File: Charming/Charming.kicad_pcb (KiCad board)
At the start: 2 copper layers, 9 parts, among them SW1 SW_Push, SW2 SW_Push, SW3 SW_Push, SW4 SW_Push, U1 ProMicro

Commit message: keyboard matrix ok
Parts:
- added D10: D, Diode_SMD:D_SOD-123, F.Cu at (156.5, 124.8)
- added D11: D, Diode_SMD:D_SOD-123, F.Cu at (162.3, 121.5)
- added D12: D, Diode_SMD:D_SOD-123, F.Cu at (156.5, 121.5)
- added D13: D, Diode_SMD:D_SOD-123, F.Cu at (150.8, 124.8)
- added D14: D, Diode_SMD:D_SOD-123, F.Cu at (145.0, 124.8)
- added D15: D, Diode_SMD:D_SOD-123, F.Cu at (139.3, 131.5)
- added D16: D, Diode_SMD:D_SOD-123, F.Cu at (150.8, 121.5)
- added D17: D, Diode_SMD:D_SOD-123, F.Cu at (133.5, 131.5)
- added D18: D, Diode_SMD:D_SOD-123, F.Cu at (127.8, 131.5)
- added D19: D, Diode_SMD:D_SOD-123, F.Cu at (139.3, 128.2)
- added D20: D, Diode_SMD:D_SOD-123, F.Cu at (133.5, 128.2)
- added D21: D, Diode_SMD:D_SOD-123, F.Cu at (139.3, 124.8)
- added D22: D, Diode_SMD:D_SOD-123, F.Cu at (145.0, 121.5)
- added D23: D, Diode_SMD:D_SOD-123, F.Cu at (139.3, 121.5)
- added D24: D, Diode_SMD:D_SOD-123, F.Cu at (133.5, 124.8)
- added D25: D, Diode_SMD:D_SOD-123, F.Cu at (127.8, 128.2)
- added D26: D, Diode_SMD:D_SOD-123, F.Cu at (122.0, 131.5)
- added D27: D, Diode_SMD:D_SOD-123, F.Cu at (133.5, 121.5)
- added D28: D, Diode_SMD:D_SOD-123, F.Cu at (116.3, 131.5)
- added D29: D, Diode_SMD:D_SOD-123, F.Cu at (110.5, 131.5)
- added D30: D, Diode_SMD:D_SOD-123, F.Cu at (122.0, 128.2)
- added D31: D, Diode_SMD:D_SOD-123, F.Cu at (116.3, 128.2)
- added D32: D, Diode_SMD:D_SOD-123, F.Cu at (127.8, 124.8)
- added D33: D, Diode_SMD:D_SOD-123, F.Cu at (122.0, 124.8)
- added D34: D, Diode_SMD:D_SOD-123, F.Cu at (127.8, 121.5)
- added D35: D, Diode_SMD:D_SOD-123, F.Cu at (122.0, 121.5)
- added D36: D, Diode_SMD:D_SOD-123, F.Cu at (116.3, 124.8)
- added D37: D, Diode_SMD:D_SOD-123, F.Cu at (110.5, 128.2)
- added D38: D, Diode_SMD:D_SOD-123, F.Cu at (116.3, 121.5)
- added D39: D, Diode_SMD:D_SOD-123, F.Cu at (104.8, 131.5)
- added D40: D, Diode_SMD:D_SOD-123, F.Cu at (99.0, 131.5)
- added D41: D, Diode_SMD:D_SOD-123, F.Cu at (104.8, 128.2)
- added D42: D, Diode_SMD:D_SOD-123, F.Cu at (99.0, 128.2)
- added D43: D, Diode_SMD:D_SOD-123, F.Cu at (110.5, 124.8)
- added D44: D, Diode_SMD:D_SOD-123, F.Cu at (110.5, 121.5)
- added D45: D, Diode_SMD:D_SOD-123, F.Cu at (104.8, 124.8)
- added D46: D, Diode_SMD:D_SOD-123, F.Cu at (99.0, 124.8)
- added D47: D, Diode_SMD:D_SOD-123, F.Cu at (104.8, 121.5)
- added D48: D, Diode_SMD:D_SOD-123, F.Cu at (99.0, 121.5)
- added D5: D, Diode_SMD:D_SOD-123, F.Cu at (150.8, 131.5)
- added D6: D, Diode_SMD:D_SOD-123, F.Cu at (145.0, 131.5)
- added D7: D, Diode_SMD:D_SOD-123, F.Cu at (156.5, 128.2)
- added D8: D, Diode_SMD:D_SOD-123, F.Cu at (150.8, 128.2)
- added D9: D, Diode_SMD:D_SOD-123, F.Cu at (145.0, 128.2)
- added SW10: SW_Push, keyswitches:SW_PG1350, F.Cu at (218.5, 38.0)
- added SW11: SW_Push, keyswitches:SW_PG1350, F.Cu at (237.5, 38.0)
- added SW12: SW_Push, keyswitches:SW_PG1350, F.Cu at (256.5, 38.0)
- added SW13: SW_Push, keyswitches:SW_PG1350, F.Cu at (42.8, 57.0)
- added SW14: SW_Push, keyswitches:SW_PG1350, F.Cu at (61.8, 57.0)
- added SW15: SW_Push, keyswitches:SW_PG1350, F.Cu at (80.8, 57.0)
- added SW16: SW_Push, keyswitches:SW_PG1350, F.Cu at (99.8, 57.0)
- added SW17: SW_Push, keyswitches:SW_PG1350, F.Cu at (118.8, 57.0)
- added SW18: SW_Push, keyswitches:SW_PG1350, F.Cu at (137.8, 57.0)
- added SW19: SW_Push, keyswitches:SW_PG1350, F.Cu at (166.2, 57.0)
- added SW20: SW_Push, keyswitches:SW_PG1350, F.Cu at (185.2, 57.0)
- added SW21: SW_Push, keyswitches:SW_PG1350, F.Cu at (204.2, 57.0)
- added SW22: SW_Push, keyswitches:SW_PG1350, F.Cu at (223.2, 57.0)
- added SW23: SW_Push, keyswitches:SW_PG1350, F.Cu at (242.2, 57.0)
- added SW24: SW_Push, keyswitches:SW_PG1350, F.Cu at (261.2, 57.0)
- added SW25: SW_Push, keyswitches:SW_PG1350, F.Cu at (38.0, 76.0)
- added SW26: SW_Push, keyswitches:SW_PG1350, F.Cu at (57.0, 76.0)
- added SW27: SW_Push, keyswitches:SW_PG1350, F.Cu at (76.0, 76.0)
- added SW28: SW_Push, keyswitches:SW_PG1350, F.Cu at (95.0, 76.0)
- added SW29: SW_Push, keyswitches:SW_PG1350, F.Cu at (114.0, 76.0)
- added SW30: SW_Push, keyswitches:SW_PG1350, F.Cu at (133.0, 76.0)
- added SW31: SW_Push, keyswitches:SW_PG1350, F.Cu at (171.0, 76.0)
- added SW32: SW_Push, keyswitches:SW_PG1350, F.Cu at (190.0, 76.0)
- added SW33: SW_Push, keyswitches:SW_PG1350, F.Cu at (209.0, 76.0)
- added SW34: SW_Push, keyswitches:SW_PG1350, F.Cu at (228.0, 76.0)
- added SW35: SW_Push, keyswitches:SW_PG1350, F.Cu at (247.0, 76.0)
- added SW36: SW_Push, keyswitches:SW_PG1350, F.Cu at (266.0, 76.0)
- added SW37: SW_Push, keyswitches:SW_PG1350, F.Cu at (47.5, 95.0)
- added SW38: SW_Push, keyswitches:SW_PG1350, F.Cu at (66.5, 95.0)
- added SW39: SW_Push, keyswitches:SW_PG1350, F.Cu at (85.5, 95.0)
- added SW40: SW_Push, keyswitches:SW_PG1350, F.Cu at (104.5, 95.0)
- added SW41: SW_Push, keyswitches:SW_PG1350, F.Cu at (128.2, 95.0)
- added SW42: SW_Push, keyswitches:SW_PG1350, F.Cu at (152.0, 76.0)
- added SW43: SW_Push, keyswitches:SW_PG1350, F.Cu at (152.0, 95.0)
- added SW44: SW_Push, keyswitches:SW_PG1350, F.Cu at (175.8, 95.0)
- added SW45: SW_Push, keyswitches:SW_PG1350, F.Cu at (199.5, 95.0)
- added SW46: SW_Push, keyswitches:SW_PG1350, F.Cu at (218.5, 95.0)
- added SW47: SW_Push, keyswitches:SW_PG1350, F.Cu at (237.5, 95.0)
- added SW48: SW_Push, keyswitches:SW_PG1350, F.Cu at (256.5, 95.0)
- added SW5: SW_Push, keyswitches:SW_PG1350, F.Cu at (123.5, 38.0)
- added SW6: SW_Push, keyswitches:SW_PG1350, F.Cu at (142.5, 38.0)
- added SW7: SW_Push, keyswitches:SW_PG1350, F.Cu at (161.5, 38.0)
- added SW8: SW_Push, keyswitches:SW_PG1350, F.Cu at (180.5, 38.0)
- added SW9: SW_Push, keyswitches:SW_PG1350, F.Cu at (199.5, 38.0)
- moved SW1 152.4 mm to (47.5, 38.0)
- moved SW2 151.9 mm to (66.5, 38.0)
- moved U1 146.2 mm to (19.0, 52.2)
- moved SW4 140.1 mm to (104.5, 38.0)
- moved SW3 138.1 mm to (85.5, 38.0)
- moved D4 31.3 mm to (168.0, 121.5), turned to 0 degrees
- moved D2 27.5 mm to (162.3, 124.8), turned to 0 degrees
- moved D3 19.4 mm to (156.5, 131.5), turned to 0 degrees
- moved D1 13.7 mm to (168.0, 124.8), turned to 0 degrees
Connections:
- D2 pad 1: row1 -> row0
- D4 pad 1: row1 -> row0
- SW2 pad 1: col0 -> col1
- SW3 pad 1: col1 -> col2
- SW4 pad 1: col1 -> col3
- U1 pad 10: Net-(U1-Pad10) -> col6
- U1 pad 11: Net-(U1-Pad11) -> col5
- U1 pad 12: Net-(U1-Pad12) -> col4
- U1 pad 13: Net-(U1-Pad13) -> col3
- U1 pad 14: Net-(U1-Pad14) -> col2
- U1 pad 15: Net-(U1-Pad15) -> col1
- U1 pad 16: Net-(U1-Pad16) -> col0
- U1 pad 17: col1 -> row3
- U1 pad 18: col0 -> row2
- U1 pad 5: Net-(U1-Pad5) -> col11
- U1 pad 6: Net-(U1-Pad6) -> col10
- U1 pad 7: Net-(U1-Pad7) -> col9
- U1 pad 8: Net-(U1-Pad8) -> col8
- U1 pad 9: Net-(U1-Pad9) -> col7
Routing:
- net col1: track 70.4 -> 0.00 mm
- net col0: track 50.9 -> 0.00 mm
- net row1: track 37.3 -> 0.00 mm
- net row0: track 35.5 -> 0.00 mm
- net GND: track 18.8 -> 0.00 mm
- net Net-(D2-Pad2): track 6.06 -> 0.00 mm
- net Net-(D1-Pad2): track 5.83 -> 0.00 mm
- net Net-(D4-Pad2): track 5.68 -> 0.00 mm
- net Net-(D3-Pad2): track 5.68 -> 0.00 mm

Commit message: all components on but routing failed
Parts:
- moved D1 160.0 mm to (41.4, 27.0), turned to 270 degrees
- moved D36 153.6 mm to (259.9, 70.2), turned to 270 degrees
- moved D48 150.2 mm to (248.4, 105.8), turned to 270 degrees
- moved D2 144.9 mm to (55.4, 27.0), turned to 270 degrees
- moved D24 138.9 mm to (249.7, 48.6), turned to 270 degrees
- moved D13 137.9 mm to (35.1, 49.9), turned to 270 degrees
- moved D12 132.7 mm to (249.7, 27.0), turned to 270 degrees
- moved D3 132.1 mm to (75.7, 27.0), turned to 270 degrees
- moved D35 130.5 mm to (242.1, 70.2), turned to 270 degrees
- moved D47 128.1 mm to (231.9, 105.8), turned to 270 degrees
- moved D46 121.7 mm to (219.2, 105.8), turned to 270 degrees
- moved D4 120.3 mm to (93.5, 27.0), turned to 270 degrees
- moved D14 117.8 mm to (54.1, 49.9), turned to 270 degrees
- moved D23 116.9 mm to (230.6, 48.6), turned to 270 degrees
- moved D11 116.6 mm to (230.6, 27.0), turned to 270 degrees
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
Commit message: 3d view is back
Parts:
- D1, D10, D11, D12, D2, D3, D4, D5, D6, D7, D8, D9: moved to B.Cu
- moved D6 2.54 mm to (135.4, 25.8), turned to 90 degrees
- turned D1 to 90 degrees
- turned D10 to 90 degrees
- turned D11 to 90 degrees
- turned D12 to 90 degrees
- turned D2 to 90 degrees
- turned D3 to 90 degrees
- turned D4 to 90 degrees
- turned D5 to 90 degrees
- turned D7 to 90 degrees
- turned D8 to 90 degrees
- turned D9 to 90 degrees
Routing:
- net row3: track 0.00 -> 341.4 mm, vias 0 -> 1
- net col11: track 0.00 -> 315.3 mm
- net row0: track 0.00 -> 303.2 mm
- net col10: track 0.00 -> 293.6 mm
- net col9: track 0.00 -> 275.3 mm
- net row2: track 0.00 -> 260.1 mm, vias 0 -> 1
- net col8: track 0.00 -> 254.9 mm
- net col7: track 0.00 -> 247.1 mm
- net row1: track 0.00 -> 230.8 mm, vias 0 -> 1
- net col6: track 0.00 -> 230.3 mm
- net col5: track 0.00 -> 191.3 mm
- net col4: track 0.00 -> 177.8 mm
- net col3: track 0.00 -> 141.8 mm
- net col2: track 0.00 -> 123.7 mm
- net col1: track 0.00 -> 100.3 mm
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
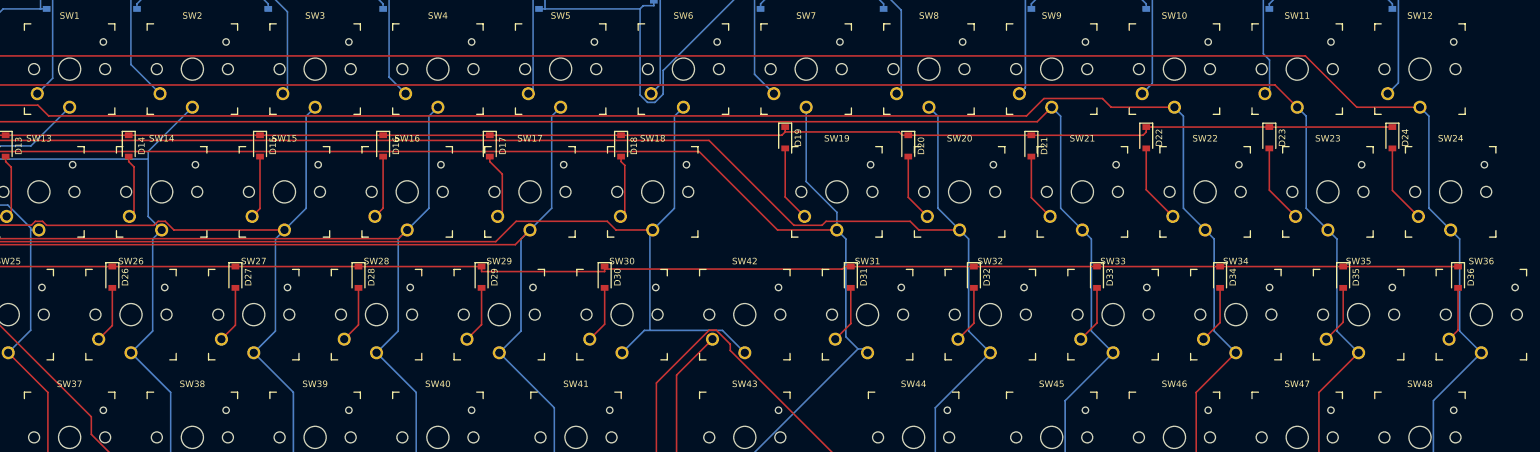
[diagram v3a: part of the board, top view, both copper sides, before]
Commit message: update PG13500 footprint
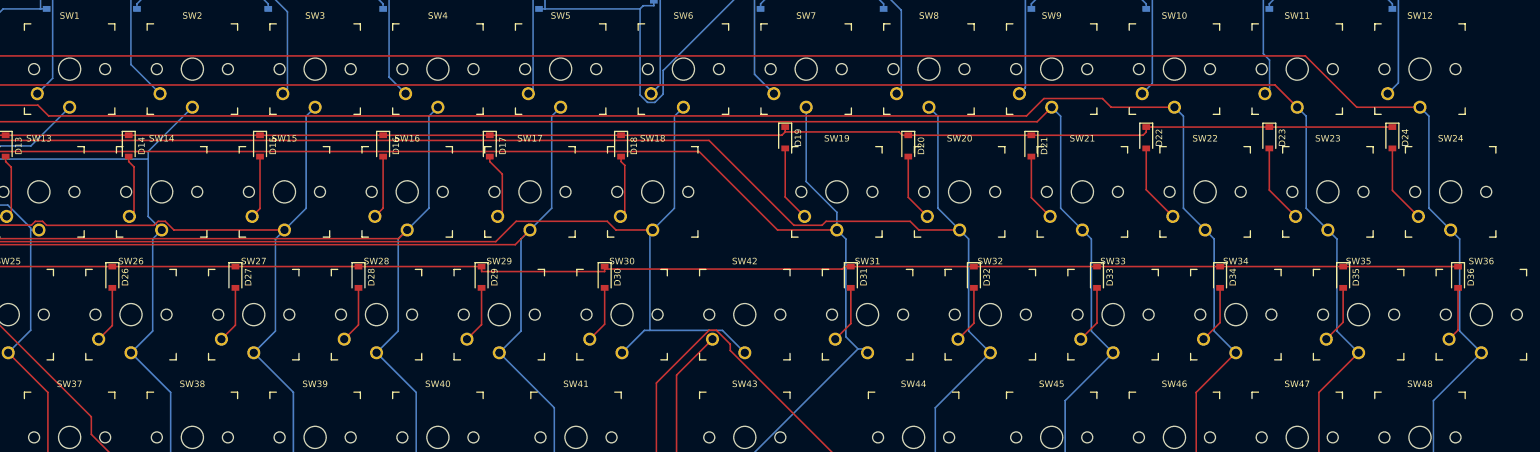
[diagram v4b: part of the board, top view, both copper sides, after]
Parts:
- SW1, SW10, SW11, SW12, SW13, SW14, SW15, SW16, SW17, SW18, SW19, SW2, SW20, SW21, SW22, SW23, SW24, SW25, SW26, SW27, SW28, SW29, SW3, SW30, SW31, SW32, SW33, SW34, SW35, SW36, SW37, SW38, SW39, SW4, SW40, SW41, SW42, SW43, SW44, SW45, SW46, SW47, SW48, SW5, SW6, SW7, SW8, SW9: footprint keyswitches:SW_PG1350 -> Charming:SW_PG1350
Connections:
- D10 pad 1: row0 -> row1
- D11 pad 1: row0 -> row2
- D12 pad 1: row0 -> row3
- D13 pad 1: row1 -> row0
- D15 pad 1: row1 -> row2
- D16 pad 1: row1 -> row3
- D17 pad 1: row1 -> row0
- D19 pad 1: row1 -> row2
- D2 pad 1: row0 -> row1
- D20 pad 1: row1 -> row3
- D21 pad 1: row1 -> row0
- D23 pad 1: row1 -> row2
- D24 pad 1: row1 -> row3
- D25 pad 1: row2 -> row0
- D26 pad 1: row2 -> row1
- D28 pad 1: row2 -> row3
- D29 pad 1: row2 -> row0
- D3 pad 1: row0 -> row2
- D30 pad 1: row2 -> row1
- D32 pad 1: row2 -> row3
- D33 pad 1: row2 -> row0
- D34 pad 1: row2 -> row1
- D36 pad 1: row2 -> row3
- D37 pad 1: row3 -> row0
- D38 pad 1: row3 -> row1
- D39 pad 1: row3 -> row2
- D4 pad 1: row0 -> row3
- D41 pad 1: row3 -> row0
- D42 pad 1: row3 -> row1
- D43 pad 1: row3 -> row2
- D45 pad 1: row3 -> row0
- D46 pad 1: row3 -> row1
- D47 pad 1: row3 -> row2
- D6 pad 1: row0 -> row1
- D7 pad 1: row0 -> row2
- D8 pad 1: row0 -> row3
- SW10 pad 1: col9 -> col2
- SW11 pad 1: col10 -> col2
- SW12 pad 1: col11 -> col2
- SW13 pad 1: col0 -> col3
- SW14 pad 1: col1 -> col3
- SW15 pad 1: col2 -> col3
- SW18 pad 1: col5 -> col4
- SW19 pad 1: col6 -> col4
- SW2 pad 1: col1 -> col0
- SW20 pad 1: col7 -> col4
- SW21 pad 1: col8 -> col5
- SW22 pad 1: col9 -> col5
- SW23 pad 1: col10 -> col5
- SW24 pad 1: col11 -> col5
- SW25 pad 1: col0 -> col6
- SW26 pad 1: col1 -> col6
- SW27 pad 1: col2 -> col6
- SW28 pad 1: col3 -> col6
- SW29 pad 1: col4 -> col7
- SW3 pad 1: col2 -> col0
- SW30 pad 1: col5 -> col7
- SW31 pad 1: col6 -> col7
- SW34 pad 1: col9 -> col8
- SW35 pad 1: col10 -> col8
- SW36 pad 1: col11 -> col8
- SW37 pad 1: col0 -> col9
- SW38 pad 1: col1 -> col9
- SW39 pad 1: col2 -> col9
- SW4 pad 1: col3 -> col0
- SW40 pad 1: col3 -> col9
- SW41 pad 1: col4 -> col10
- SW42 pad 1: col5 -> col10
- SW43 pad 1: col6 -> col10
- SW44 pad 1: col7 -> col10
- SW45 pad 1: col8 -> col11
- SW46 pad 1: col9 -> col11
- SW47 pad 1: col10 -> col11
- SW5 pad 1: col4 -> col1
- SW6 pad 1: col5 -> col1
- SW7 pad 1: col6 -> col1
- SW8 pad 1: col7 -> col1
- SW9 pad 1: col8 -> col2

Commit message: before row col changle
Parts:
- D1, D10, D11, D12, D2, D3, D4, D5, D6, D7, D8, D9: moved to F.Cu
- moved D42 32.2 mm to (140.0, 73.6)
- moved D43 26.8 mm to (140.0, 92.6)
- moved D37 22.1 mm to (35.5, 92.6)
- moved D40 21.6 mm to (92.5, 92.6)
- moved D39 21.1 mm to (73.5, 92.6)
- moved D38 21.1 mm to (54.5, 92.6)
- moved D41 20.5 mm to (111.5, 92.6)
- moved D44 19.0 mm to (166.1, 92.6)
- moved D46 18.3 mm to (206.5, 92.6)
- moved D45 18.3 mm to (187.5, 92.6)
- moved D47 14.6 mm to (225.5, 92.6)
- moved D48 13.7 mm to (244.5, 92.6)
- moved D6 10.8 mm to (130.5, 35.4), turned to 270 degrees
- moved D9 10.5 mm to (187.5, 35.4), turned to 270 degrees
- moved D1 10.4 mm to (35.2, 35.4), turned to 270 degrees
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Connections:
- D10 pad 1: row1 -> row0
- D11 pad 1: row2 -> row0
- D12 pad 1: row3 -> row0
- D13 pad 1: row0 -> row1
- D15 pad 1: row2 -> row1
- D16 pad 1: row3 -> row1
- D17 pad 1: row0 -> row1
- D19 pad 1: row2 -> row1
- D2 pad 1: row1 -> row0
- D20 pad 1: row3 -> row1
- D21 pad 1: row0 -> row1
- D23 pad 1: row2 -> row1
- D24 pad 1: row3 -> row1
- D25 pad 1: row0 -> row2
- D26 pad 1: row1 -> row2
- D28 pad 1: row3 -> row2
- D29 pad 1: row0 -> row2
- D3 pad 1: row2 -> row0
- D30 pad 1: row1 -> row2
- D32 pad 1: row3 -> row2
- D33 pad 1: row0 -> row2
- D34 pad 1: row1 -> row2
- D36 pad 1: row3 -> row2
- D37 pad 1: row0 -> row3
- D38 pad 1: row1 -> row3
- D39 pad 1: row2 -> row3
- D4 pad 1: row3 -> row0
- D41 pad 1: row0 -> row3
- D42 pad 1: row1 -> row3
- D43 pad 1: row2 -> row3
- D45 pad 1: row0 -> row3
- D46 pad 1: row1 -> row3
- D47 pad 1: row2 -> row3
- D6 pad 1: row1 -> row0
- D7 pad 1: row2 -> row0
- D8 pad 1: row3 -> row0
- SW10 pad 1: col2 -> col9
- SW11 pad 1: col2 -> col10
- SW12 pad 1: col2 -> col11
- SW13 pad 1: col3 -> col0
- SW14 pad 1: col3 -> col1
- SW15 pad 1: col3 -> col2
- SW18 pad 1: col4 -> col5
- SW19 pad 1: col4 -> col6
- SW2 pad 1: col0 -> col1
- SW20 pad 1: col4 -> col7
- SW21 pad 1: col5 -> col8
- SW22 pad 1: col5 -> col9
- SW23 pad 1: col5 -> col10
- SW24 pad 1: col5 -> col11
- SW25 pad 1: col6 -> col0
- SW26 pad 1: col6 -> col1
- SW27 pad 1: col6 -> col2
- SW28 pad 1: col6 -> col3
- SW29 pad 1: col7 -> col4
- SW3 pad 1: col0 -> col2
- SW30 pad 1: col7 -> col5
- SW31 pad 1: col7 -> col6
- SW34 pad 1: col8 -> col9
- SW35 pad 1: col8 -> col10
- SW36 pad 1: col8 -> col11
- SW37 pad 1: col9 -> col0
- SW38 pad 1: col9 -> col1
- SW39 pad 1: col9 -> col2
- SW4 pad 1: col0 -> col3
- SW40 pad 1: col9 -> col3
- SW41 pad 1: col10 -> col4
- SW42 pad 1: col10 -> col5
- SW43 pad 1: col10 -> col6
- SW44 pad 1: col10 -> col7
- SW45 pad 1: col11 -> col8
- SW46 pad 1: col11 -> col9
- SW47 pad 1: col11 -> col10
- SW5 pad 1: col1 -> col4
- SW6 pad 1: col1 -> col5
- SW7 pad 1: col1 -> col6
- SW8 pad 1: col1 -> col7
- SW9 pad 1: col2 -> col8
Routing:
- net row3: track 341.4 -> 0.00 mm, vias 1 -> 0
- net col11: track 315.3 -> 0.00 mm
- net row0: track 303.2 -> 0.00 mm
- net col10: track 293.6 -> 0.00 mm
- net col9: track 275.3 -> 0.00 mm
- net row2: track 260.1 -> 0.00 mm, vias 1 -> 0
- net col8: track 254.9 -> 0.00 mm
- net col7: track 247.1 -> 0.00 mm
- net row1: track 230.8 -> 0.00 mm, vias 1 -> 0
- net col6: track 230.3 -> 0.00 mm
- net col5: track 191.3 -> 0.00 mm
- net col4: track 177.8 -> 0.00 mm
- net col3: track 141.8 -> 0.00 mm
- net col2: track 123.7 -> 0.00 mm
- net col1: track 100.3 -> 0.00 mm
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
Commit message: v1
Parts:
- moved D29 46.5 mm to (131.5, 109.6)
- moved D30 46.5 mm to (150.5, 109.6)
- moved D25 46.5 mm to (55.5, 109.6)
- moved D28 46.5 mm to (112.5, 109.6)
- moved D26 46.5 mm to (74.5, 109.6)
- moved D27 46.5 mm to (93.5, 109.6)
- moved D42 45.9 mm to (150.5, 118.3), turned to 90 degrees
- moved U1 41.8 mm to (26.5, 84.0)
- moved D1 37.5 mm to (45.7, 71.4)
- moved D10 37.5 mm to (217.0, 71.4)
- moved D11 37.5 mm to (236.0, 71.4)
- moved D12 37.5 mm to (255.0, 71.4)
- moved D13 37.5 mm to (41.2, 89.1)
- moved D14 37.5 mm to (60.2, 89.1)
- moved D15 37.5 mm to (79.2, 89.1)
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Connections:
- U1 pad 11: col5 -> row2
- U1 pad 12: col4 -> row3
- U1 pad 13: col3 -> col5
- U1 pad 14: col2 -> col4
- U1 pad 15: col1 -> col3
- U1 pad 16: col0 -> col2
- U1 pad 17: row3 -> col1
- U1 pad 18: row2 -> col0
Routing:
- net col11: track 0.00 -> 317.7 mm
- net col10: track 0.00 -> 292.7 mm
- net col9: track 0.00 -> 283.4 mm
- net col8: track 0.00 -> 262.8 mm
- net row3: track 0.00 -> 256.4 mm
- net row2: track 0.00 -> 252.4 mm
- net col7: track 0.00 -> 246.0 mm
- net col6: track 0.00 -> 228.2 mm
- net row1: track 0.00 -> 227.6 mm
- net row0: track 0.00 -> 225.2 mm
- net col5: track 0.00 -> 172.8 mm
- net col4: track 0.00 -> 161.4 mm
- net col3: track 0.00 -> 142.1 mm
- net col2: track 0.00 -> 123.3 mm
- net col1: track 0.00 -> 102.5 mm
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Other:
- board outline added: 269.2 x 77.5 mm

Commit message: add switch and promicro courtyard
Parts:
- moved D29 19.1 mm to (112.4, 109.6)
- moved D30 19.1 mm to (131.4, 109.6)
- moved D25 19.1 mm to (36.4, 109.6)
- moved D26 19.0 mm to (55.4, 109.6)
- moved D27 19.0 mm to (74.4, 109.6)
- moved D28 19.0 mm to (93.4, 109.6)
- moved U1 2.86 mm to (27.9, 81.5)
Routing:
- net row2: track 252.4 -> 275.7 mm
- net Net-(D29-Pad2): track 16.8 -> 6.88 mm
- net Net-(D28-Pad2): track 16.8 -> 6.88 mm
- net Net-(D27-Pad2): track 16.8 -> 6.88 mm
- net Net-(D25-Pad2): track 16.8 -> 6.88 mm
- net Net-(D26-Pad2): track 16.8 -> 6.88 mm
- net Net-(D30-Pad2): track 16.8 -> 6.88 mm
- net col0: track 91.9 -> 82.1 mm
- net col9: track 283.4 -> 274.1 mm
- net col7: track 246.0 -> 241.5 mm
- net col1: track 102.5 -> 106.4 mm
- net col11: track 317.7 -> 314.8 mm
- net row0: track 225.2 -> 222.8 mm
- net col2: track 123.3 -> 121.2 mm
- net row3: track 256.4 -> 258.3 mm
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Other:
- net class Default: clearance 0.2 -> 0.127; trace_width 0.25 -> 0.127; via_dia 0.8 -> 0.6; via_drill 0.4 -> 0.3
- rule pad_to_mask_clearance: 0.05 -> 0
- rule trace_clearance: 0.2 -> 0.127
- rule trace_min: 0.2 -> 0.127
- rule via_min_size: 0.4 -> 0.6
